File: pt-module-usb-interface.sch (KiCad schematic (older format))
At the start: 9 parts

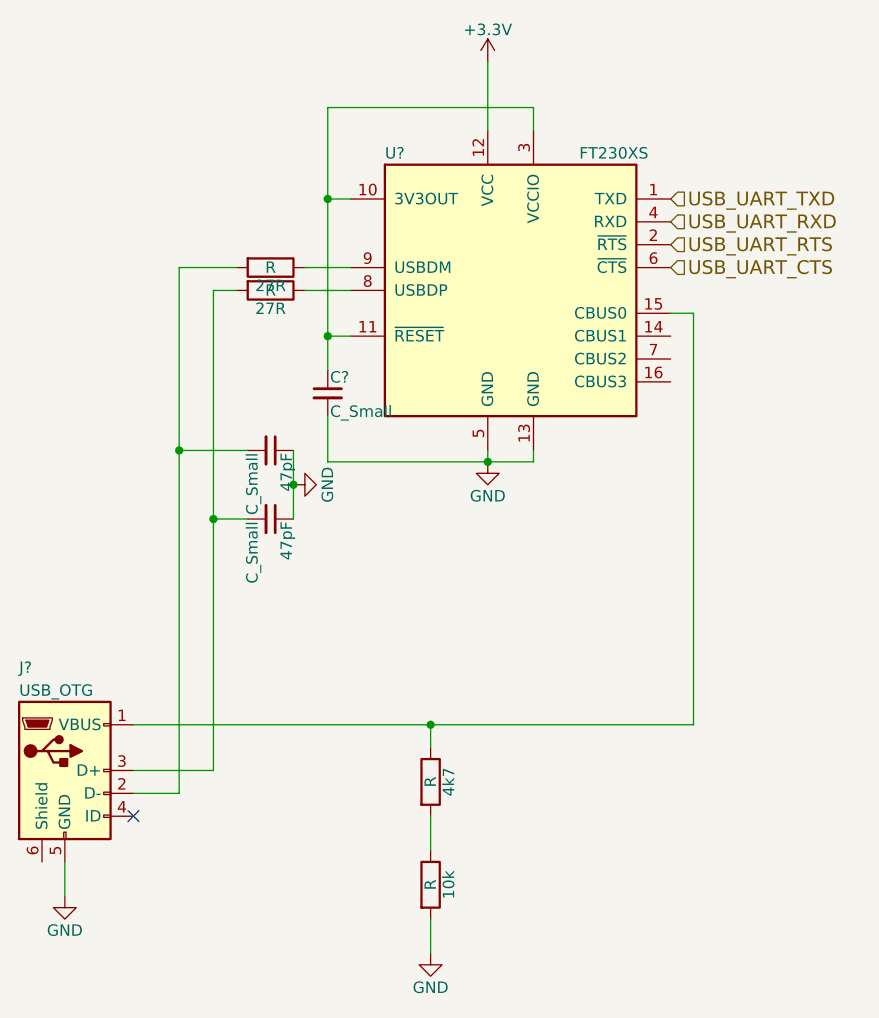
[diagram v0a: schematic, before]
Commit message: Fixed vusb_sense connection mistake
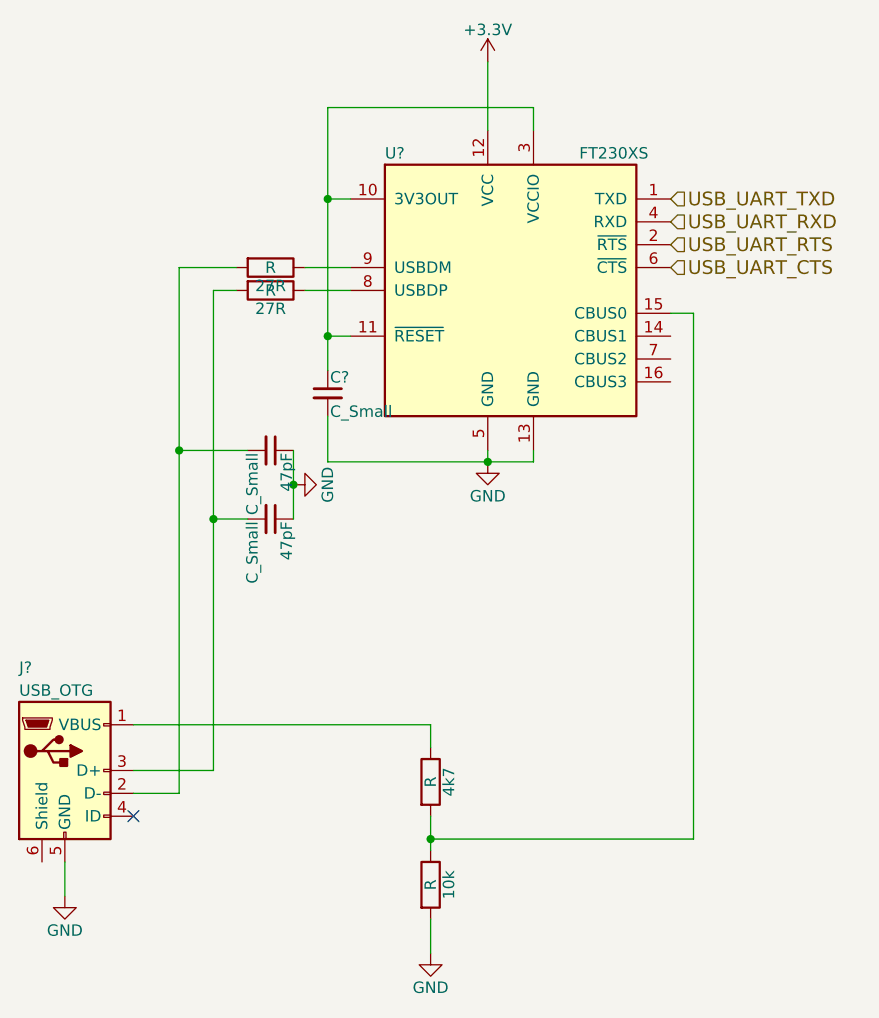
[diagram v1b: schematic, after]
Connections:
- net at 4k7.1, J?.1 (VBUS): no longer U?.15 (CBUS0)
- net at 10k.1, 4k7.2: now also U?.15 (CBUS0)
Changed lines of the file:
@@
 $EndComp
-Wire Wire Line
-	4100 4650 6550 4650
 Wire Wire Line
 	5400 5500 5400 5650
@@
 	6450 2850 6550 2850
 Wire Wire Line
-	6550 2850 6550 4650
-Connection ~ 5400 4650
+	6550 2850 6550 5150
 Connection ~ 4950 2950
 Wire Wire Line
@@
 Text HLabel 6450 2650 2    60   Input ~ 0
 USB_UART_CTS
+Wire Wire Line
+	5400 4650 4100 4650
+Wire Wire Line
+	6550 5150 5400 5150
+Connection ~ 5400 5150
 $EndSCHEMATC

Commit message: I made a connect
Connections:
- net +3V3: now also C?.1, U?.10 (3V3OUT), U?.11 (~RESET), U?.3 (VCCIO)
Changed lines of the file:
@@
 $Descr A4 11693 8268
 encoding utf-8
-Sheet 8 8
+Sheet 8 12
 Title ""
 Date ""
@@
 $EndComp
 $Comp
-L GND #PWR?
+L GND #PWR055
 U 1 1 59837539
 P 5400 5650
-F 0 "#PWR?" H 5400 5400 50  0001 C CNN
+F 0 "#PWR055" H 5400 5400 50  0001 C CNN
 F 1 "GND" H 5400 5500 50  0000 C CNN
 F 2 "" H 5400 5650 50  0001 C CNN
@@
 $EndComp
 $Comp
-L GND #PWR?
+L GND #PWR056
 U 1 1 59837659
 P 3800 5400
-F 0 "#PWR?" H 3800 5150 50  0001 C CNN
+F 0 "#PWR056" H 3800 5150 50  0001 C CNN
 F 1 "GND" H 3800 5250 50  0000 C CNN
 F 2 "" H 3800 5400 50  0001 C CNN
@@
 NoConn ~ 4100 5050
 $Comp
-L +3.3V #PWR?
+L +3.3V #PWR057
 U 1 1 59837A65
 P 5650 1750
-F 0 "#PWR?" H 5650 1600 50  0001 C CNN
+F 0 "#PWR057" H 5650 1600 50  0001 C CNN
 F 1 "+3.3V" H 5650 1890 50  0000 C CNN
 F 2 "" H 5650 1750 50  0001 C CNN
@@
 $EndComp
 $Comp
-L GND #PWR?
+L GND #PWR058
 U 1 1 59838D4F
 P 4800 3600
-F 0 "#PWR?" H 4800 3350 50  0001 C CNN
+F 0 "#PWR058" H 4800 3350 50  0001 C CNN
 F 1 "GND" H 4800 3450 50  0000 C CNN
 F 2 "" H 4800 3600 50  0001 C CNN
@@
 Connection ~ 5650 3500
 $Comp
-L GND #PWR?
+L GND #PWR059
 U 1 1 59839F17
 P 5650 3500
-F 0 "#PWR?" H 5650 3250 50  0001 C CNN
+F 0 "#PWR059" H 5650 3250 50  0001 C CNN
 F 1 "GND" H 5650 3350 50  0000 C CNN
 F 2 "" H 5650 3500 50  0001 C CNN
@@
 	6550 5150 5400 5150
 Connection ~ 5400 5150
+Connection ~ 5650 1950
 $EndSCHEMATC
